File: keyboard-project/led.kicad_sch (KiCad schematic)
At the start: 0 parts

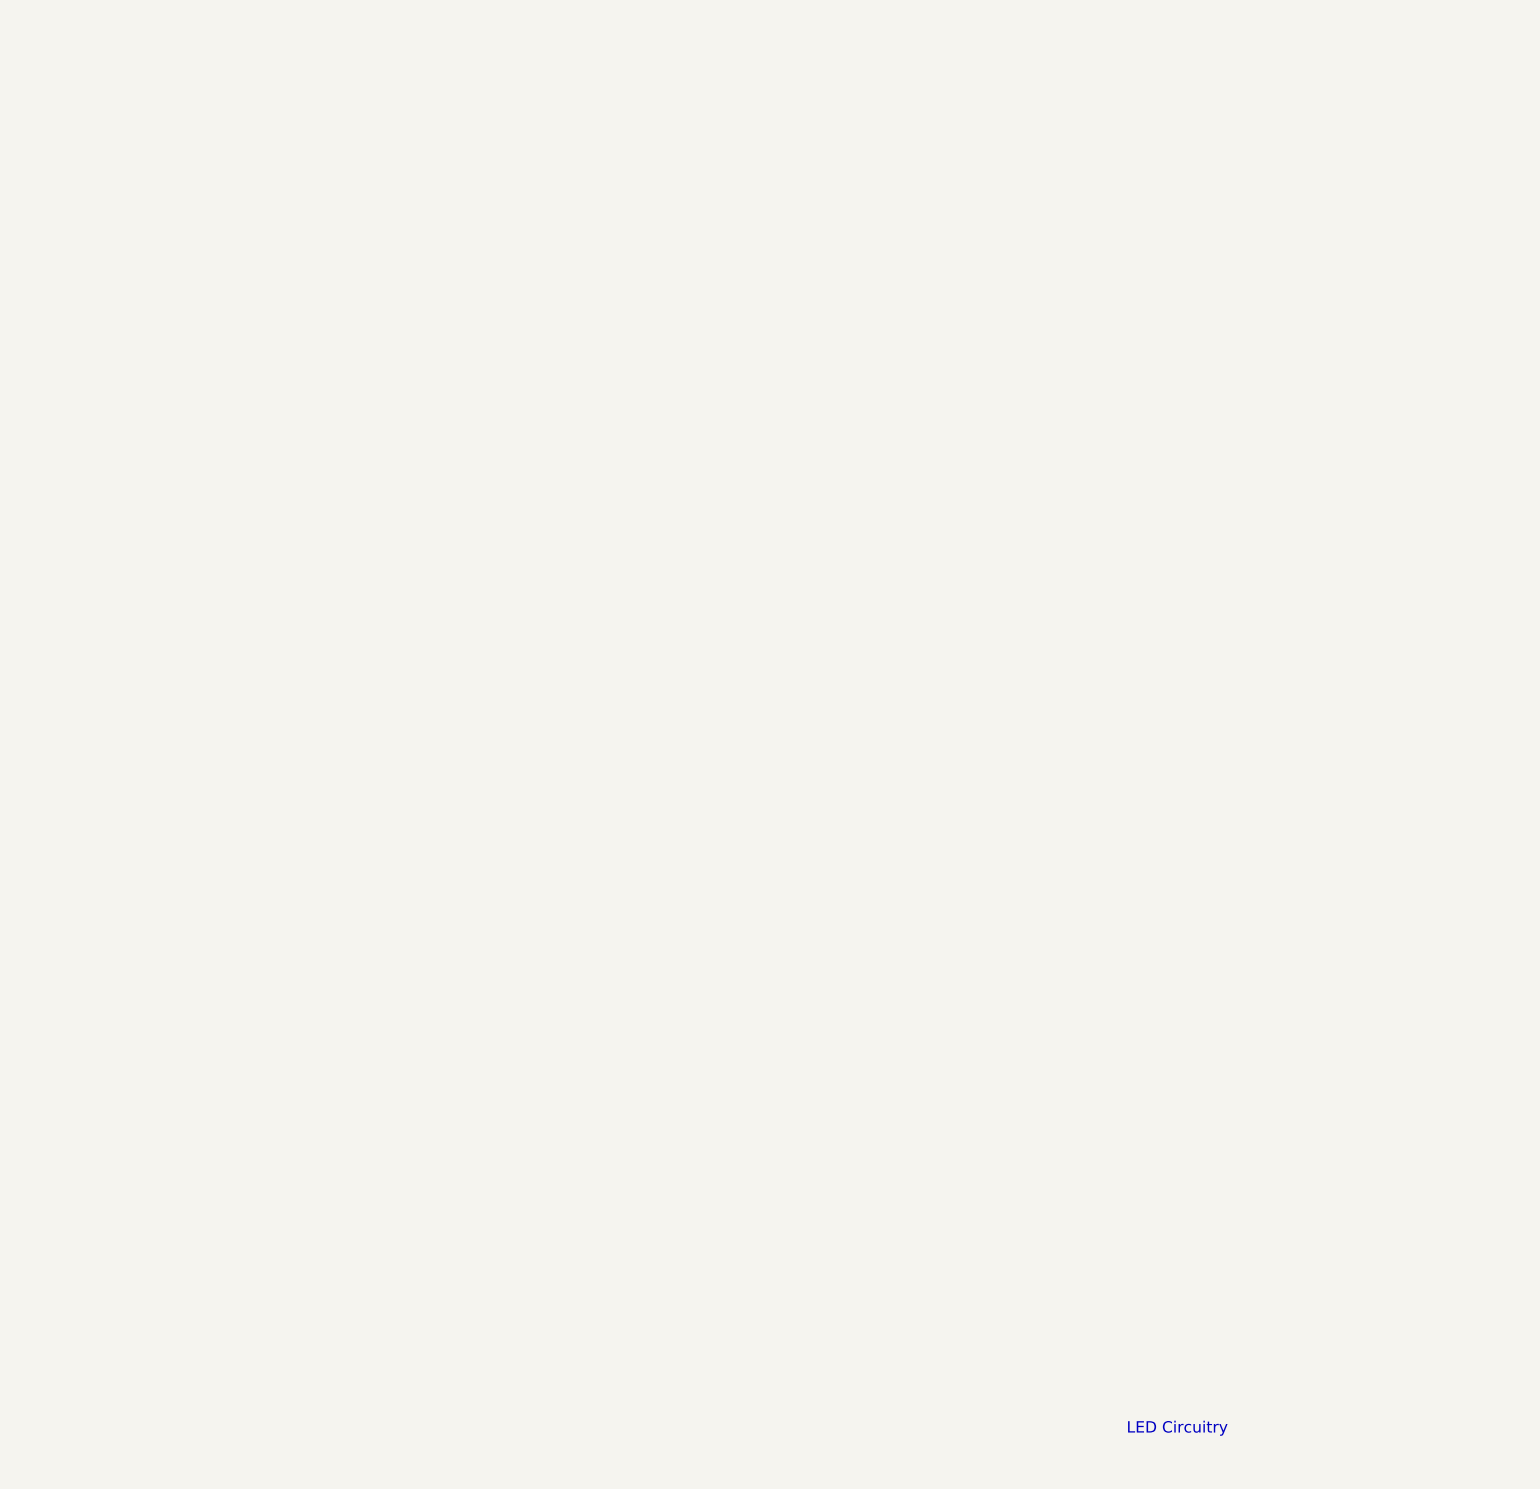
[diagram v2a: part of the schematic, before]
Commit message: encoders, trackball, and display circuits
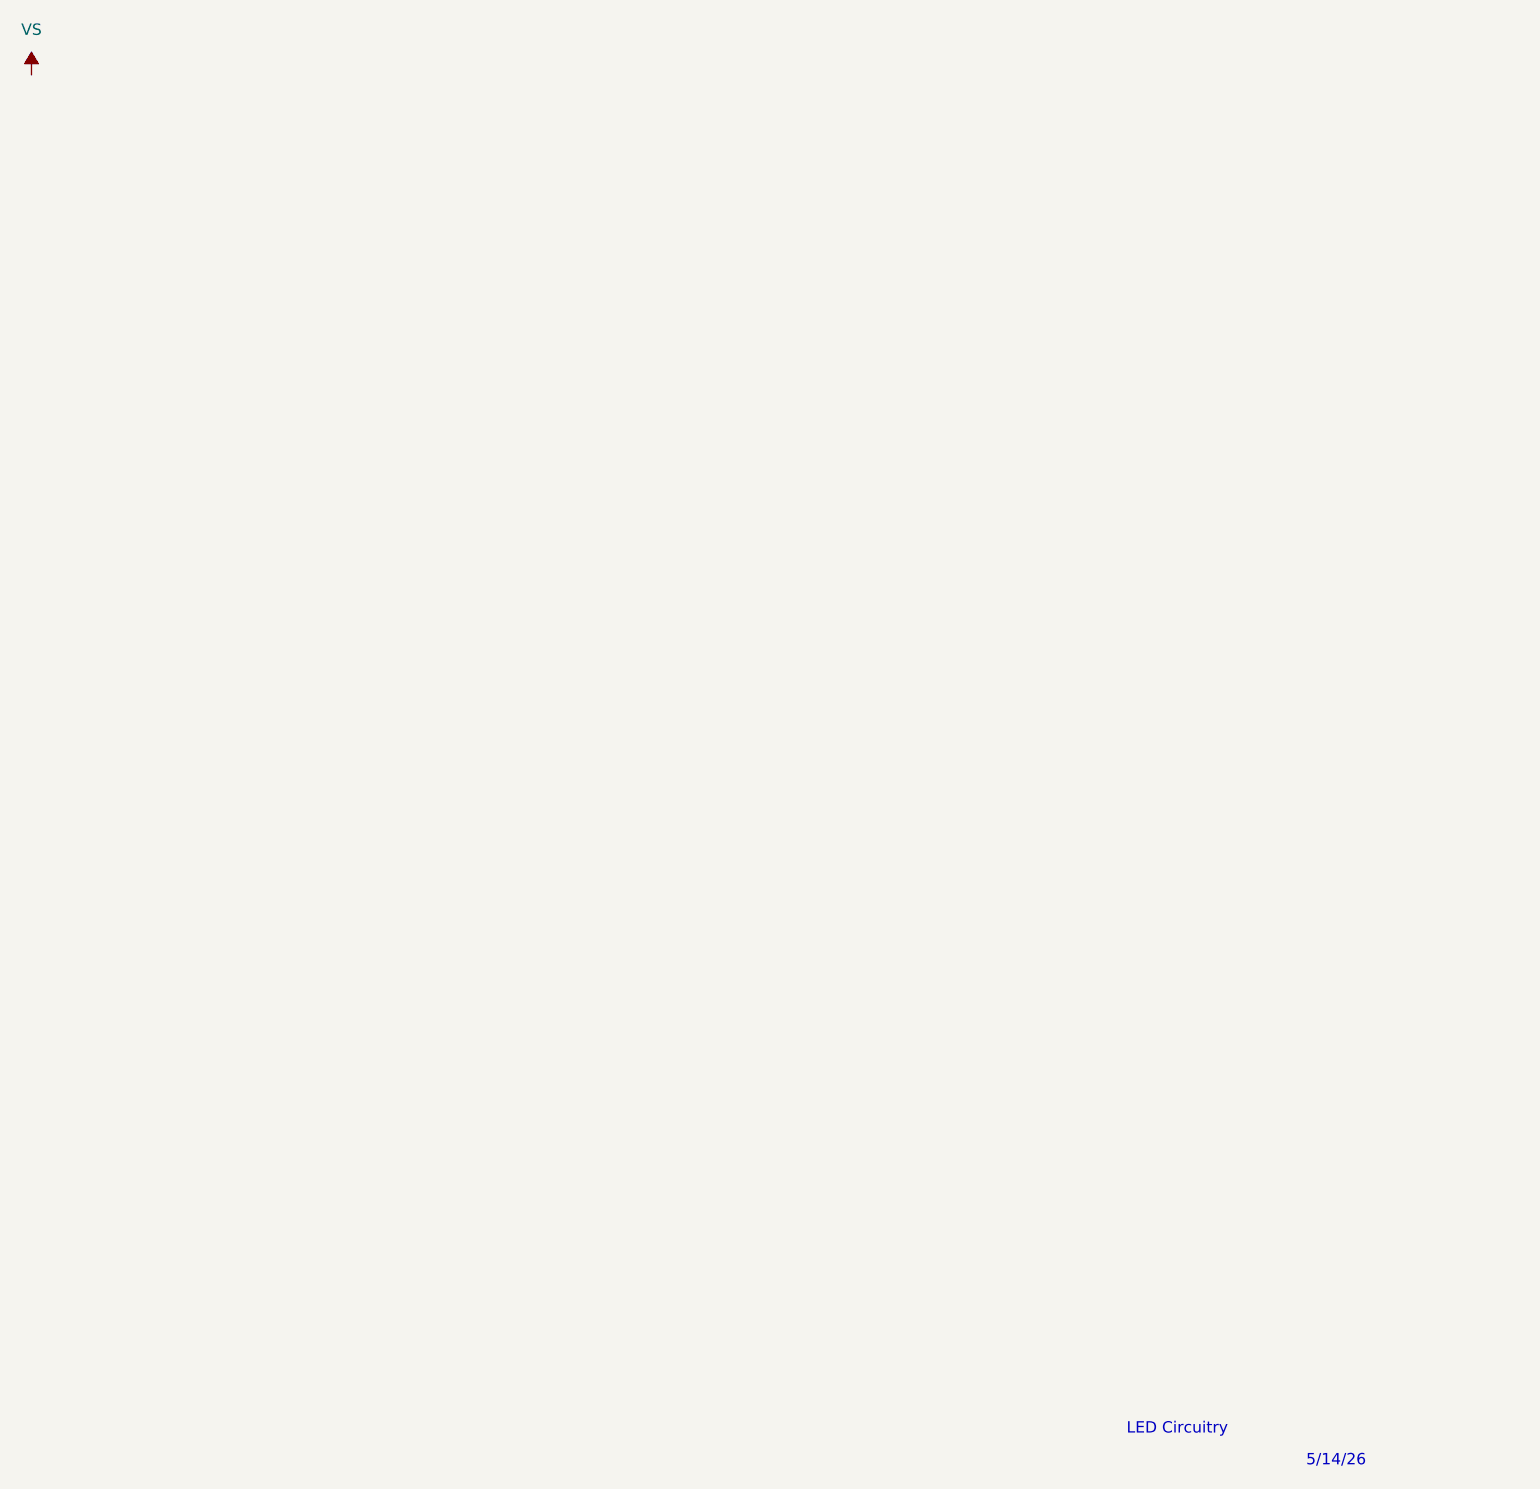
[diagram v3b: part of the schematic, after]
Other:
- note added: "5/14/26"
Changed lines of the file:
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@@
+		)
+	)
+	(text "5/14/26"
+		(exclude_from_sim no)
+		(at 210.82 193.294 0)
+		(effects
+			(font
+				(size 1.27 1.27)
+			)
+		)
+	)
+	(symbol
+		(lib_id "power:VS")
+		(at 64.77 38.1 0)
+		(unit 1)
+		(body_style 1)
+		(exclude_from_sim no)
+		(in_bom yes)
+		(on_board yes)
+		(in_pos_files yes)
+		(dnp no)
+		(fields_autoplaced yes)
+		(property "Reference" "#PWR0100"
+			(at 64.77 41.91 0)
+			(hide yes)
+			(show_name no)
+			(do_not_autoplace no)
+			(effects
+				(font
+					(size 1.27 1.27)
+				)
+			)
+		)
+		(property "Value" "VS"
+			(at 64.77 33.02 0)
+			(show_name no)
+			(do_not_autoplace no)
+			(effects
+				(font
+					(size 1.27 1.27)
+				)
+			)
+		)
+		(property "Footprint" ""
+			(at 64.77 38.1 0)
+			(hide yes)
+			(show_name no)
+			(do_not_autoplace no)
+			(effects
+				(font
+					(size 1.27 1.27)
+				)
+			)
+		)
+		(property "Datasheet" ""
+			(at 64.77 38.1 0)
+			(hide yes)
+			(show_name no)
+			(do_not_autoplace no)
+			(effects
+				(font
+					(size 1.27 1.27)
+				)
+			)
+		)
+		(property "Description" "Power symbol creates a global label with name \"VS\""
+			(at 64.77 38.1 0)
+			(hide yes)
+			(show_name no)
+			(do_not_autoplace no)
+			(effects
+				(font
+					(size 1.27 1.27)
+				)
+			)
+		)
+		(pin "1"
+		)
+		(instances
+			(project "keyboard-project"
+				(path "/20839dd3-8f37-4bf9-a231-e8a616316450/880c2070-d9f9-48e1-89be-a8d8c96f41ea"
+					(reference "#PWR0100")
+					(unit 1)
+				)
+			)
 		)
 	)

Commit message: led page
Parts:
- added D105, D106, D107, D108, D109, D110, D111, D112, D113, D114, D115, D116, D117, D118, D119, D120, D121, D122: LED_RGBA, symbol Device:LED_RGBA
- added R12: 39k, symbol Device:R_US
- added U8: IS31FL3741AQFLS4TR, IS31FL3741AQFLS4TR:QFN40P700X700X80-61N, symbol IS31FL3741AQFLS4TR:IS31FL3741AQFLS4TR
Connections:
- new net: R12.2, U8.13 (ISET)
- new net +3.3V: U8.14 (AVCC)
- new net CS1: D105.1 (RK), D106.1 (RK), D107.1 (RK), D108.1 (RK), D109.1 (RK), D110.1 (RK), D111.1 (RK), D112.1 (RK), D113.1 (RK), U8.26 (CS1)
- new net CS10: U8.35 (CS10)
- new net CS11: U8.37 (CS11)
- new net CS12: U8.38 (CS12)
- new net CS13: U8.39 (CS13)
- new net CS14: U8.40 (CS14)
- new net CS15: U8.41 (CS15)
- new net CS16: U8.42 (CS16)
- new net CS17: U8.43 (CS17)
- new net CS18: U8.44 (CS18)
- new net CS19: U8.45 (CS19)
- new net CS2: D105.2 (GK), D106.2 (GK), D107.2 (GK), D108.2 (GK), D109.2 (GK), D110.2 (GK), D111.2 (GK), D112.2 (GK), D113.2 (GK), U8.27 (CS2)
- new net CS20: U8.46 (CS20)
- new net CS21: U8.47 (CS21)
- new net CS22: U8.48 (CS22)
- new net CS23: U8.49 (CS23)
- new net CS24: U8.50 (CS24)
- new net CS25: U8.51 (CS25)
- new net CS26: U8.52 (CS26)
- new net CS27: U8.53 (CS27)
- new net CS28: U8.54 (CS28)
- new net CS29: U8.56 (CS29)
- new net CS3: D105.3 (BK), D106.3 (BK), D107.3 (BK), D108.3 (BK), D109.3 (BK), D110.3 (BK), D111.3 (BK), D112.3 (BK), D113.3 (BK), U8.28 (CS3)
- new net CS30: U8.57 (CS30)
- new net CS31: U8.58 (CS31)
- new net CS32: U8.59 (CS32)
- new net CS33: U8.60 (CS33)
- new net CS34: U8.1 (CS34)
- new net CS35: U8.2 (CS35)
- new net CS36: U8.3 (CS36)
- new net CS37: D114.1 (RK), D115.1 (RK), D116.1 (RK), D117.1 (RK), D118.1 (RK), D119.1 (RK), D120.1 (RK), D121.1 (RK), D122.1 (RK), U8.4 (CS37)
- new net CS38: D114.2 (GK), D115.2 (GK), D116.2 (GK), D117.2 (GK), D118.2 (GK), D119.2 (GK), D120.2 (GK), D121.2 (GK), D122.2 (GK), U8.5 (CS38)
- new net CS39: D114.3 (BK), D115.3 (BK), D116.3 (BK), D117.3 (BK), D118.3 (BK), D119.3 (BK), D120.3 (BK), D121.3 (BK), D122.3 (BK), U8.6 (CS39)
- new net CS4: U8.29 (CS4)
- new net CS5: U8.30 (CS5)
- new net CS6: U8.31 (CS6)
- new net CS7: U8.32 (CS7)
- new net CS8: U8.33 (CS8)
- new net CS9: U8.34 (CS9)
- new net GND: R12.1, U8.12 (GND), U8.36 (GND), U8.55 (GND), U8.61 (EXP), U8.8 (ADDR)
- new net I2C1_SCL: U8.10 (SCL)
- new net I2C1_SDA: U8.9 (SDA)
- new net IS31FL3741A SDB: U8.11 (SDB)
- new net PVCC: U8.15 (PVCC), U8.25 (PVCC)
- new net SW1: D105.4 (A), D114.4 (A), U8.16 (SW1)
- new net SW2: D106.4 (A), D115.4 (A), U8.17 (SW2)
- new net SW3: D107.4 (A), D116.4 (A), U8.18 (SW3)
- new net SW4: D108.4 (A), D117.4 (A), U8.19 (SW4)
- new net SW5: D109.4 (A), D118.4 (A), U8.20 (SW5)
- new net SW6: D110.4 (A), D119.4 (A), U8.21 (SW6)
- new net SW7: D111.4 (A), D120.4 (A), U8.22 (SW7)
- new net SW8: D112.4 (A), D121.4 (A), U8.23 (SW8)
- new net SW9: D113.4 (A), D122.4 (A), U8.24 (SW9)
- no-connect marks 0 -> 1
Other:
- note added: "5/17/26"
- note added: "9 X 13 = 117 LEDS WIRING AS THIS: PICK 1: SW[1-9] PICK 1: CS[N,N+1,N+2] N = 1, 4, 7, ..., 37"
- note removed: "5/14/26"

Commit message: res and cap footprints
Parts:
- R12: footprint (none) -> Resistor_SMD:R_1206_3216Metric_Pad1.30x1.75mm_HandSolder
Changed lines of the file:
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@@
 			)
 		)
-		(property "Footprint" ""
+		(property "Footprint" "Resistor_SMD:R_1206_3216Metric_Pad1.30x1.75mm_HandSolder"
 			(at 33.274 89.154 90)
 			(hide yes)

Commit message: all footprints in now
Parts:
- added D123, D124, D125, D126, D127, D128, D129, D130, D131, D132, D133, D134, D135, D136, D137, D138, D139, D140, D141, D142, D143, D144, D145, D146, D147, D148, D149, D150, D151, D152, D153, D154, D155, D156, D157, D158, D159, D160, D161, D162, D163, D164, D165, D166, D167, D168, D169, D170, D171, D172, D173, D174, D175, D176, D177, D178, D179, D180, D181, D182, D183, D184, D185, D186, D187, D188, D189, D190, D191, D192, D193, D194, D195, D196, D197, D198, D199, D200, D201, D202, D203, D204, D205, D206, D207, D208, D209, D210, D211, D212, D213, D214, D215, D216, D217, D218, D219, D220, D221: LED_RGBA, KAA-3528RGBS-11:LED_AAA3528LSEKJ3ZGKQBKS, symbol Device:LED_RGBA
- D105, D106, D107, D108, D109, D110, D111, D112, D113, D114, D115, D116, D117, D118, D119, D120, D121, D122: footprint (none) -> KAA-3528RGBS-11:LED_AAA3528LSEKJ3ZGKQBKS
- U8: footprint IS31FL3741AQFLS4TR:QFN40P700X700X80-61N -> Package_QFP:TQFP-48-1EP_7x7mm_P0.5mm_EP4.11x4.11mm
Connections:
- net CS10: now also D141.1 (RK), D142.1 (RK), D143.1 (RK), D144.1 (RK), D145.1 (RK), D146.1 (RK), D147.1 (RK), D148.1 (RK), D149.1 (RK)
- net CS11: now also D141.2 (GK), D142.2 (GK), D143.2 (GK), D144.2 (GK), D145.2 (GK), D146.2 (GK), D147.2 (GK), D148.2 (GK), D149.2 (GK)
- net CS12: now also D141.3 (BK), D142.3 (BK), D143.3 (BK), D144.3 (BK), D145.3 (BK), D146.3 (BK), D147.3 (BK), D148.3 (BK), D149.3 (BK)
- net CS13: now also D150.1 (RK), D151.1 (RK), D152.1 (RK), D153.1 (RK), D154.1 (RK), D155.1 (RK), D156.1 (RK), D157.1 (RK), D158.1 (RK)
- net CS14: now also D150.2 (GK), D151.2 (GK), D152.2 (GK), D153.2 (GK), D154.2 (GK), D155.2 (GK), D156.2 (GK), D157.2 (GK), D158.2 (GK)
- net CS15: now also D150.3 (BK), D151.3 (BK), D152.3 (BK), D153.3 (BK), D154.3 (BK), D155.3 (BK), D156.3 (BK), D157.3 (BK), D158.3 (BK)
- net CS16: now also D159.1 (RK), D160.1 (RK), D161.1 (RK), D162.1 (RK), D163.1 (RK), D164.1 (RK), D165.1 (RK), D166.1 (RK), D167.1 (RK)
- net CS17: now also D159.2 (GK), D160.2 (GK), D161.2 (GK), D162.2 (GK), D163.2 (GK), D164.2 (GK), D165.2 (GK), D166.2 (GK), D167.2 (GK)
- net CS18: now also D159.3 (BK), D160.3 (BK), D161.3 (BK), D162.3 (BK), D163.3 (BK), D164.3 (BK), D165.3 (BK), D166.3 (BK), D167.3 (BK)
- net CS19: now also D168.1 (RK), D169.1 (RK), D170.1 (RK), D171.1 (RK), D172.1 (RK), D173.1 (RK), D174.1 (RK), D175.1 (RK), D176.1 (RK)
- net CS20: now also D168.2 (GK), D169.2 (GK), D170.2 (GK), D171.2 (GK), D172.2 (GK), D173.2 (GK), D174.2 (GK), D175.2 (GK), D176.2 (GK)
- net CS21: now also D168.3 (BK), D169.3 (BK), D170.3 (BK), D171.3 (BK), D172.3 (BK), D173.3 (BK), D174.3 (BK), D175.3 (BK), D176.3 (BK)
- net CS22: now also D177.1 (RK), D178.1 (RK), D179.1 (RK), D180.1 (RK), D181.1 (RK), D182.1 (RK), D183.1 (RK), D184.1 (RK), D185.1 (RK)
- net CS23: now also D177.2 (GK), D178.2 (GK), D179.2 (GK), D180.2 (GK), D181.2 (GK), D182.2 (GK), D183.2 (GK), D184.2 (GK), D185.2 (GK)
- net CS24: now also D177.3 (BK), D178.3 (BK), D179.3 (BK), D180.3 (BK), D181.3 (BK), D182.3 (BK), D183.3 (BK), D184.3 (BK), D185.3 (BK)
- net CS25: now also D186.1 (RK), D187.1 (RK), D188.1 (RK), D189.1 (RK), D190.1 (RK), D191.1 (RK), D192.1 (RK), D193.1 (RK), D194.1 (RK)
- net CS26: now also D186.2 (GK), D187.2 (GK), D188.2 (GK), D189.2 (GK), D190.2 (GK), D191.2 (GK), D192.2 (GK), D193.2 (GK), D194.2 (GK)
- net CS27: now also D186.3 (BK), D187.3 (BK), D188.3 (BK), D189.3 (BK), D190.3 (BK), D191.3 (BK), D192.3 (BK), D193.3 (BK), D194.3 (BK)
- net CS28: now also D195.1 (RK), D196.1 (RK), D197.1 (RK), D198.1 (RK), D199.1 (RK), D200.1 (RK), D201.1 (RK), D202.1 (RK), D203.1 (RK)
- net CS29: now also D195.2 (GK), D196.2 (GK), D197.2 (GK), D198.2 (GK), D199.2 (GK), D200.2 (GK), D201.2 (GK), D202.2 (GK), D203.2 (GK)
- net CS30: now also D195.3 (BK), D196.3 (BK), D197.3 (BK), D198.3 (BK), D199.3 (BK), D200.3 (BK), D201.3 (BK), D202.3 (BK), D203.3 (BK)
- net CS31: now also D114.1 (RK), D115.1 (RK), D116.1 (RK), D117.1 (RK), D118.1 (RK), D119.1 (RK), D120.1 (RK), D121.1 (RK), D122.1 (RK)
- net CS32: now also D114.2 (GK), D115.2 (GK), D116.2 (GK), D117.2 (GK), D118.2 (GK), D119.2 (GK), D120.2 (GK), D121.2 (GK), D122.2 (GK)
- net CS33: now also D114.3 (BK), D115.3 (BK), D116.3 (BK), D117.3 (BK), D118.3 (BK), D119.3 (BK), D120.3 (BK), D121.3 (BK), D122.3 (BK)
- net CS34: now also D204.1 (RK), D205.1 (RK), D206.1 (RK), D207.1 (RK), D208.1 (RK), D209.1 (RK), D210.1 (RK), D211.1 (RK), D212.1 (RK)
- net CS35: now also D204.2 (GK), D205.2 (GK), D206.2 (GK), D207.2 (GK), D208.2 (GK), D209.2 (GK), D210.2 (GK), D211.2 (GK), D212.2 (GK)
- net CS36: now also D204.3 (BK), D205.3 (BK), D206.3 (BK), D207.3 (BK), D208.3 (BK), D209.3 (BK), D210.3 (BK), D211.3 (BK), D212.3 (BK)
- net CS37: now also D213.1 (RK), D214.1 (RK), D215.1 (RK), D216.1 (RK), D217.1 (RK), D218.1 (RK), D219.1 (RK), D220.1 (RK), D221.1 (RK); no longer D114.1 (RK), D115.1 (RK), D116.1 (RK), D117.1 (RK), D118.1 (RK), D119.1 (RK), D120.1 (RK), D121.1 (RK), D122.1 (RK)
- net CS38: now also D213.2 (GK), D214.2 (GK), D215.2 (GK), D216.2 (GK), D217.2 (GK), D218.2 (GK), D219.2 (GK), D220.2 (GK), D221.2 (GK); no longer D114.2 (GK), D115.2 (GK), D116.2 (GK), D117.2 (GK), D118.2 (GK), D119.2 (GK), D120.2 (GK), D121.2 (GK), D122.2 (GK)
- net CS39: now also D213.3 (BK), D214.3 (BK), D215.3 (BK), D216.3 (BK), D217.3 (BK), D218.3 (BK), D219.3 (BK), D220.3 (BK), D221.3 (BK); no longer D114.3 (BK), D115.3 (BK), D116.3 (BK), D117.3 (BK), D118.3 (BK), D119.3 (BK), D120.3 (BK), D121.3 (BK), D122.3 (BK)
- net CS4: now also D123.1 (RK), D124.1 (RK), D125.1 (RK), D126.1 (RK), D127.1 (RK), D128.1 (RK), D129.1 (RK), D130.1 (RK), D131.1 (RK)
- net CS5: now also D123.2 (GK), D124.2 (GK), D125.2 (GK), D126.2 (GK), D127.2 (GK), D128.2 (GK), D129.2 (GK), D130.2 (GK), D131.2 (GK)
- net CS6: now also D123.3 (BK), D124.3 (BK), D125.3 (BK), D126.3 (BK), D127.3 (BK), D128.3 (BK), D129.3 (BK), D130.3 (BK), D131.3 (BK)
- net CS7: now also D132.1 (RK), D133.1 (RK), D134.1 (RK), D135.1 (RK), D136.1 (RK), D137.1 (RK), D138.1 (RK), D139.1 (RK), D140.1 (RK)
- net CS8: now also D132.2 (GK), D133.2 (GK), D134.2 (GK), D135.2 (GK), D136.2 (GK), D137.2 (GK), D138.2 (GK), D139.2 (GK), D140.2 (GK)
- net CS9: now also D132.3 (BK), D133.3 (BK), D134.3 (BK), D135.3 (BK), D136.3 (BK), D137.3 (BK), D138.3 (BK), D139.3 (BK), D140.3 (BK)
- net SW1: now also D123.4 (A), D132.4 (A), D141.4 (A), D150.4 (A), D159.4 (A), D168.4 (A), D177.4 (A), D186.4 (A), D195.4 (A), D204.4 (A), D213.4 (A)
- net SW2: now also D124.4 (A), D133.4 (A), D142.4 (A), D151.4 (A), D160.4 (A), D169.4 (A), D178.4 (A), D187.4 (A), D196.4 (A), D205.4 (A), D214.4 (A)
- net SW3: now also D125.4 (A), D134.4 (A), D143.4 (A), D152.4 (A), D161.4 (A), D170.4 (A), D179.4 (A), D188.4 (A), D197.4 (A), D206.4 (A), D215.4 (A)
- net SW4: now also D126.4 (A), D135.4 (A), D144.4 (A), D153.4 (A), D162.4 (A), D171.4 (A), D180.4 (A), D189.4 (A), D198.4 (A), D207.4 (A), D216.4 (A)
- net SW5: now also D127.4 (A), D136.4 (A), D145.4 (A), D154.4 (A), D163.4 (A), D172.4 (A), D181.4 (A), D190.4 (A), D199.4 (A), D208.4 (A), D217.4 (A)
- net SW6: now also D128.4 (A), D137.4 (A), D146.4 (A), D155.4 (A), D164.4 (A), D173.4 (A), D182.4 (A), D191.4 (A), D200.4 (A), D209.4 (A), D218.4 (A)
- net SW7: now also D129.4 (A), D138.4 (A), D147.4 (A), D156.4 (A), D165.4 (A), D174.4 (A), D183.4 (A), D192.4 (A), D201.4 (A), D210.4 (A), D219.4 (A)
- net SW8: now also D130.4 (A), D139.4 (A), D148.4 (A), D157.4 (A), D166.4 (A), D175.4 (A), D184.4 (A), D193.4 (A), D202.4 (A), D211.4 (A), D220.4 (A)
- net SW9: now also D131.4 (A), D140.4 (A), D149.4 (A), D158.4 (A), D167.4 (A), D176.4 (A), D185.4 (A), D194.4 (A), D203.4 (A), D212.4 (A), D221.4 (A)
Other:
- note removed: "9 X 13 = 117 LEDS WIRING AS THIS: PICK 1: SW[1-9] PICK 1: CS[N,N+1,N+2] N = 1, 4, 7, ..., 37"
- moved on the sheet: D105, R12, U8
